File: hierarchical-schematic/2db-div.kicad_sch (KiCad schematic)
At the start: 28 parts, among them J1001 Conn_01x02, J1002 From R2, J1003 Conn_01x02, J1004 Out, SW1001 2dB, SW1002 Video, U1001 MC1458, U1002 MC1458

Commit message: hierarchical schematic updated to pass erc
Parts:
- removed U1001: MC1458, 2db-div:MC1458P, symbol Device:Opamp_Dual
- removed U1002: MC1458, 2db-div:MC1458P, symbol 2db-div:MC1458P
- added U1001: MC1458P, symbol spectrum analyzer:MC1458P
- D1001: symbol 2db-div:1N4152 -> Diode:1N4152
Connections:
- net GND: now also U1001.3 (+), U1001.5 (+)
- net at D1001.2 (A), R1003.1, R1007.2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: now also U1001.6 (-)
- net at D1001.1 (K), R1011.2, R1013.1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: now also U1001.7
- net at R1005.2, R1007.1, TP1001.1: now also U1001.1
- net at R1001.1, R1003.2: now also U1001.8 (V+)
- net at C1002.2, R1002.2: now also U1001.4 (V-)
- net at R1004.2, R1005.1: now also U1001.2 (-)

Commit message: v7 conversion
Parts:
- D1001: Spice_Lib_File 2db-div-spice\fairch.lib -> (none); Spice_Model 1N4152 -> (none); Spice_Netlist_Enabled Y -> (none); Spice_Node_Sequence 2 1 -> (none); Spice_Primitive D -> (none)
- J1001, J1003: Spice_Model Conn_01x02 -> (none); Spice_Netlist_Enabled N -> (none); Spice_Primitive J -> (none)
- J1004: Spice_Model Conn_Coaxial -> (none); Spice_Netlist_Enabled N -> (none); Spice_Primitive J -> (none)
- R1006: Spice_Lib_File 2db-div-spice\Pot.lib -> (none); Spice_Model pot_lin -> (none); Spice_Netlist_Enabled Y -> (none); Spice_Primitive X -> (none)
- R1012: Spice_Lib_File 2db-div-spice\Pot2.lib -> (none); Spice_Model pot_lin2 -> (none); Spice_Netlist_Enabled Y -> (none); Spice_Primitive X -> (none)
- SW1001: value 2dB -> ${SIM.PARAMS}; Spice_Netlist_Enabled N -> (none); Spice_Primitive R -> (none)
- TP1001: value 1458 Pin 1 -> ${SIM.PARAMS}; Spice_Netlist_Enabled N -> (none)
- TP1002: value 1458 Pin 7 -> ${SIM.PARAMS}; Spice_Netlist_Enabled N -> (none)

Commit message: Update to timebase and 2lo gerbers
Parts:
- J1002: symbol Connector:Conn_01x01_Female -> Connector:Conn_01x01_Socket
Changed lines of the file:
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@@
     )
   )
-  (symbol (lib_id "Connector:Conn_01x01_Female") (at 113.03 83.82 0) (mirror y) (unit 1)
+  (symbol (lib_id "Connector:Conn_01x01_Socket") (at 113.03 83.82 0) (mirror y) (unit 1)
     (in_bom yes) (on_board yes) (dnp no) (fields_autoplaced)
     (property "Reference" "J1002" (at 113.665 78.74 0)

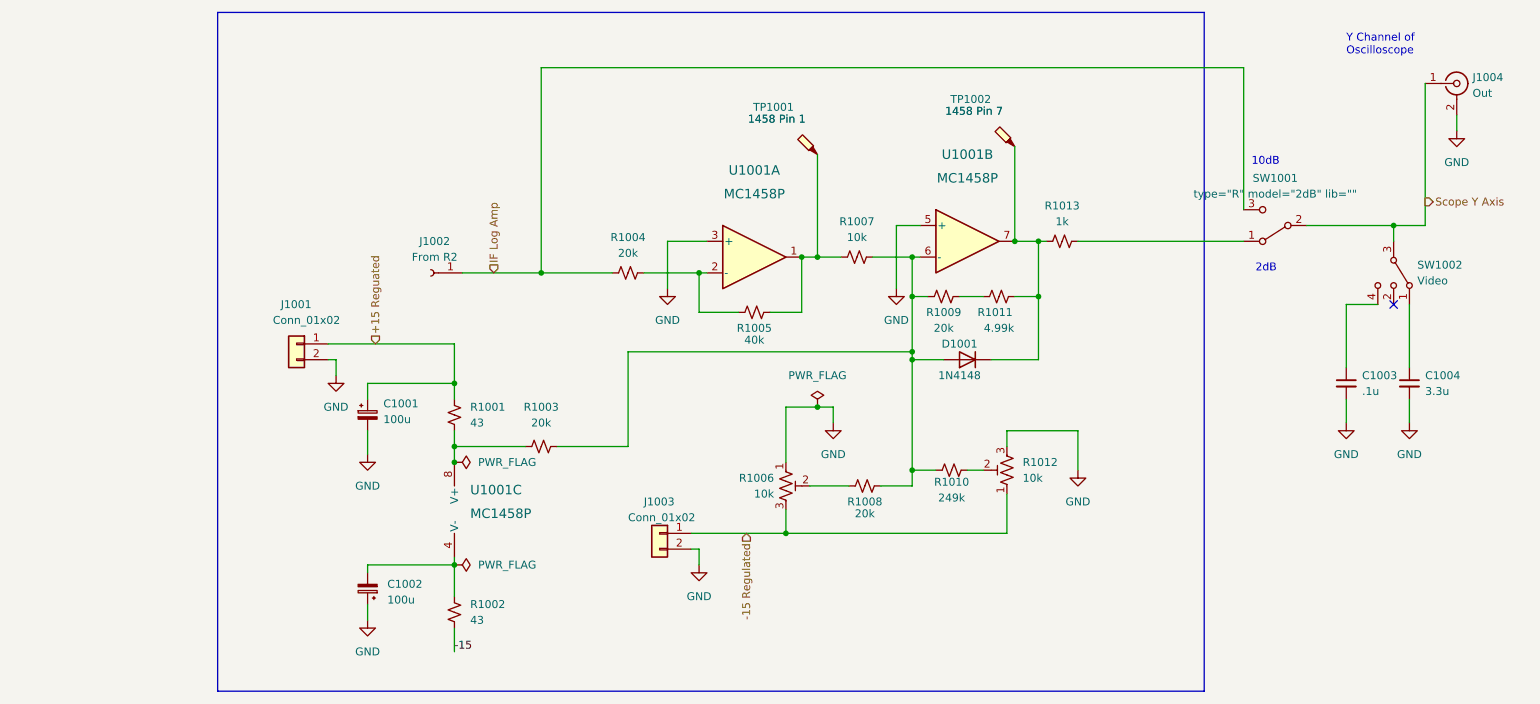
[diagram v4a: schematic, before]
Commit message: erc changes for hierarchical schematic
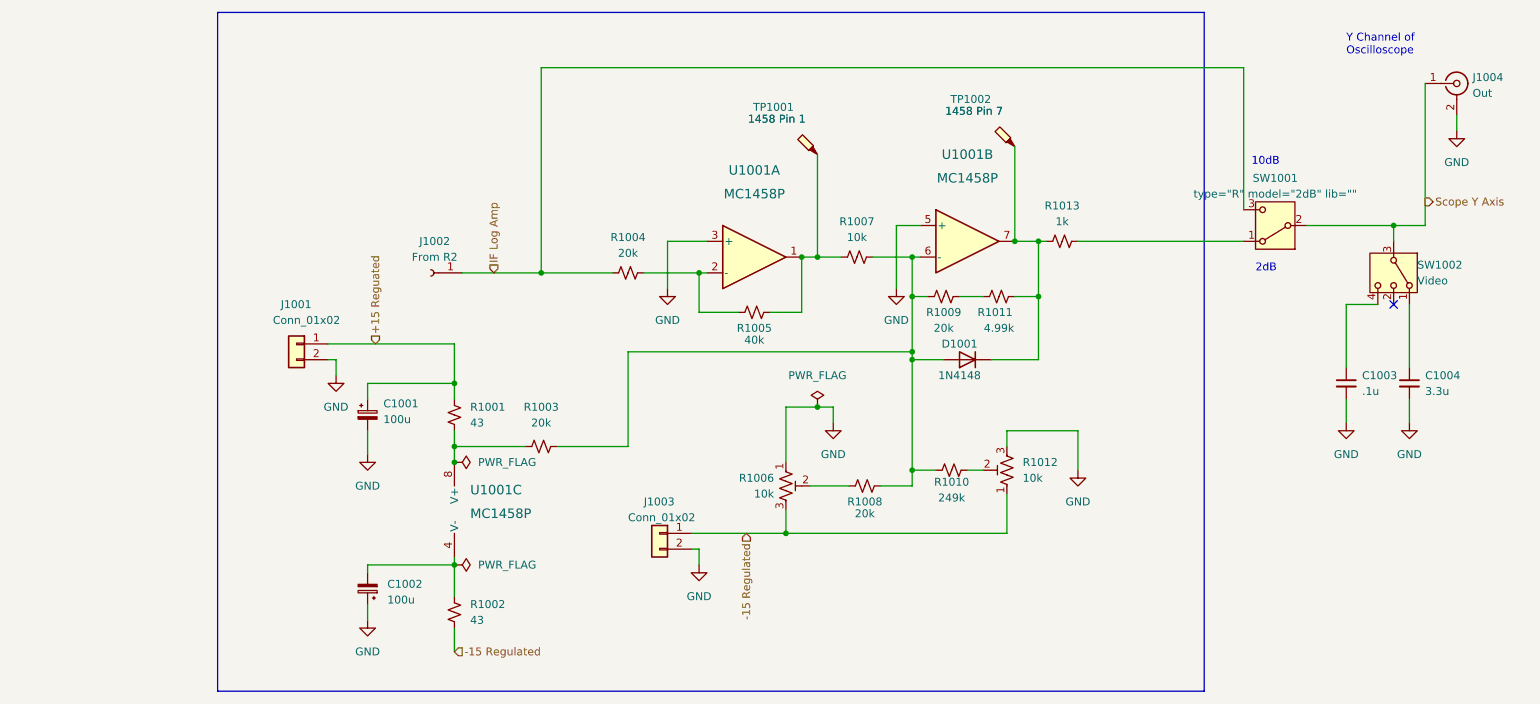
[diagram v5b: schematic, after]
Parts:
- D1001: symbol Diode:1N4152 -> Diode:1N4148
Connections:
- net -15 is gone; now on net -15 Regulated: R1002.1
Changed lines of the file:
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@@
-    (effects (font (size 1.27 1.27)) (justify left bottom))
-  )
-  (label "-15" (at 116.84 144.78 0) (fields_autoplaced)
     (effects (font (size 1.27 1.27)) (justify left bottom))
   )
@@
   )
   (hierarchical_label "IF Log Amp" (shape input) (at 123.19 83.82 90) (fields_autoplaced)
+    (effects (font (size 1.27 1.27)) (justify left))
+  )
+  (hierarchical_label "-15 Regulated" (shape input) (at 116.84 144.78 0) (fields_autoplaced)
     (effects (font (size 1.27 1.27)) (justify left))
   )
@@
     (property "Datasheet" " ~" (at 278.13 53.34 0)
       (effects (font (size 1.27 1.27)) hide)
-    )
-    (property "Sim.Enable" "0" (at 278.13 53.34 0)
-      (effects (font (size 1.27 1.27)) hide)
-    )
-    (property "Sim.Device" "SPICE" (at 278.13 53.34 0)
-      (effects (font (size 1.27 1.27)) hide)
-    )
-    (property "Sim.Params" "type=\"J\" model=\"Conn_Coaxial\" lib=\"\"" (at 0 0 0)
-      (effects (font (size 0 0)) hide)
-    )
-    (property "Sim.Pins" "1=1 2=2" (at 0 0 0)
-      (effects (font (size 0 0)) hide)
     )
     (pin "1")
@@
     )
   )
-  (symbol (lib_id "Diode:1N4152") (at 199.39 97.79 180) (unit 1)
+  (symbol (lib_id "Diode:1N4148") (at 199.39 97.79 180) (unit 1)
     (in_bom yes) (on_board yes) (dnp no)
     (property "Reference" "D1001" (at 198.12 95.25 0)
@@
       (effects (font (size 1.27 1.27)))
     )
-    (property "Footprint" "Diode_THT:D_DO-35_SOD27_P7.62mm_Horizontal" (at 199.39 93.345 0)
-      (effects (font (size 1.27 1.27)) hide)
-    )
-    (property "Datasheet" "" (at 199.39 97.79 0)
-      (effects (font (size 1.27 1.27)) hide)
-    )
-    (property "Sim.Device" "SPICE" (at 199.39 97.79 0)
+    (property "Footprint" "Diode_THT:D_DO-35_SOD27_P7.62mm_Horizontal" (at 199.39 97.79 0)
+      (effects (font (size 1.27 1.27)) hide)
+    )
+    (property "Datasheet" "https://assets.nexperia.com/documents/data-sheet/1N4148_1N4448.pdf" (at 199.39 97.79 0)
+      (effects (font (size 1.27 1.27)) hide)
+    )
+    (property "Sim.Device" "D" (at 199.39 97.79 0)
       (effects (font (size 1.27 1.27)) hide)
     )
@@
       (effects (font (size 0 0)) hide)
     )
-    (property "Sim.Pins" "2=1 1=2" (at 199.39 97.79 0)
-      (effects (font (size 1.27 1.27)) hide)
-    )
+    (property "Sim.Pins" "1=K 2=A" (at 199.39 97.79 0)
+      (effects (font (size 1.27 1.27)) hide)
+    )

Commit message: Added R2
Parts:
- added R2: R_Potentiometer_US, symbol Device:R_Potentiometer_US
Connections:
- net GND: now also R2.3
- net IF Log Amp: now also R2.1; no longer J1002.1 (Pin_1), R1004.1, SW1001.3 (C)
- new net: J1002.1 (Pin_1), R1004.1, R2.2, SW1001.3 (C)
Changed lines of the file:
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@@
   (junction (at 156.21 83.82) (diameter 0) (color 0 0 0 0)
+  )
+  (junction (at 118.11 83.82) (diameter 0) (color 0 0 0 0)
   )
   (no_connect (at 267.97 88.9))
@@
     (stroke (width 0) (type default))
   )
+  (wire (pts (xy 71.12 62.23) (xy 71.12 64.77))
+    (stroke (width 0) (type default))
+  )
   (wire (pts (xy 102.87 132.08) (xy 102.87 130.81))
     (stroke (width 0) (type default))
@@
     (stroke (width 0) (type default))
   )
+  (wire (pts (xy 118.11 68.58) (xy 74.93 68.58))
+    (stroke (width 0) (type default))
+  )
   (wire (pts (xy 154.94 125.73) (xy 170.18 125.73))
     (stroke (width 0) (type default))
@@
     (stroke (width 0) (type default))
   )
+  (wire (pts (xy 71.12 72.39) (xy 71.12 77.47))
+    (stroke (width 0) (type default))
+  )
   (wire (pts (xy 267.97 76.2) (xy 273.05 76.2))
     (stroke (width 0) (type default))
   )
   (wire (pts (xy 177.8 105.41) (xy 177.8 107.95))
+    (stroke (width 0) (type default))
+  )
+  (wire (pts (xy 118.11 83.82) (xy 118.11 68.58))
     (stroke (width 0) (type default))
   )
@@
     (effects (font (size 1.27 1.27)) (justify right))
   )
-  (hierarchical_label "IF Log Amp" (shape input) (at 123.19 83.82 90) (fields_autoplaced)
+  (hierarchical_label "IF Log Amp" (shape input) (at 71.12 62.23 90) (fields_autoplaced)
     (effects (font (size 1.27 1.27)) (justify left))
   )
@@
     )
   )
+  (symbol (lib_id "Device:R_Potentiometer_US") (at 71.12 68.58 0) (unit 1)
+    (in_bom yes) (on_board yes) (dnp no) (fields_autoplaced)
+    (property "Reference" "R2" (at 68.58 67.31 0)
+      (effects (font (size 1.27 1.27)) (justify right))
+    )
+    (property "Value" "R_Potentiometer_US" (at 68.58 69.85 0)
+      (effects (font (size 1.27 1.27)) (justify right))
+    )
+    (property "Footprint" "" (at 71.12 68.58 0)
+      (effects (font (size 1.27 1.27)) hide)
+    )
+    (property "Datasheet" "~" (at 71.12 68.58 0)
+      (effects (font (size 1.27 1.27)) hide)
+    )
+    (pin "3")
+    (pin "2")
+    (pin "1")
+    (instances
+      (project "W7ZOI Spectrum Analyzer"
+        (path "/d5173421-a214-4849-aa93-f108d8644c8a/6702cb80-1bae-4aa2-9f4a-d16d8c775e6d"
+          (reference "R2") (unit 1)
+        )
+      )
+    )
+  )
   (symbol (lib_id "power:GND") (at 260.35 107.95 0) (unit 1)
     (in_bom yes) (on_board yes) (dnp no) (fields_autoplaced)
@@
         )
       )
+    )
+  )
+  (symbol (lib_id "power:GND") (at 71.12 77.47 0) (unit 1)
+    (in_bom yes) (on_board yes) (dnp no) (fields_autoplaced)
+    (property "Reference" "#PWR0224" (at 71.12 83.82 0)
+      (effects (font (size 1.27 1.27)) hide)
+    )
+    (property "Value" "GND" (at 71.12 82.55 0)
+      (effects (font (size 1.27 1.27)))
+    )
+    (property "Footprint" "" (at 71.12 77.47 0)
+      (effects (font (size 1.27 1.27)) hide)
+    )
+    (property "Datasheet" "" (at 71.12 77.47 0)
+      (effects (font (size 1.27 1.27)) hide)
+    )
+    (pin "1")
+    (instances
+      (project "W7ZOI Spectrum Analyzer"
+        (path "/d5173421-a214-4849-aa93-f108d8644c8a/6702cb80-1bae-4aa2-9f4a-d16d8c775e6d"
+          (reference "#PWR0224") (unit 1)
+        )
+      )

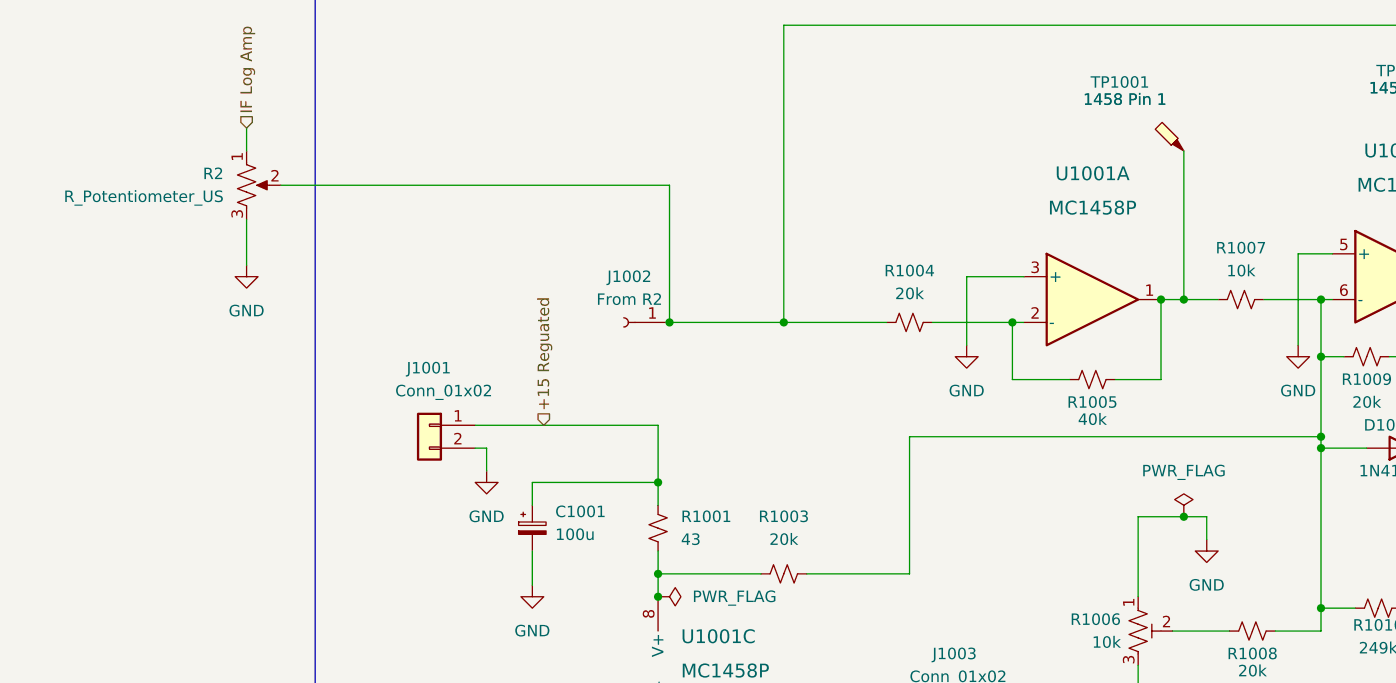
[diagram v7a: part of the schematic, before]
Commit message: updatess to kicad v8
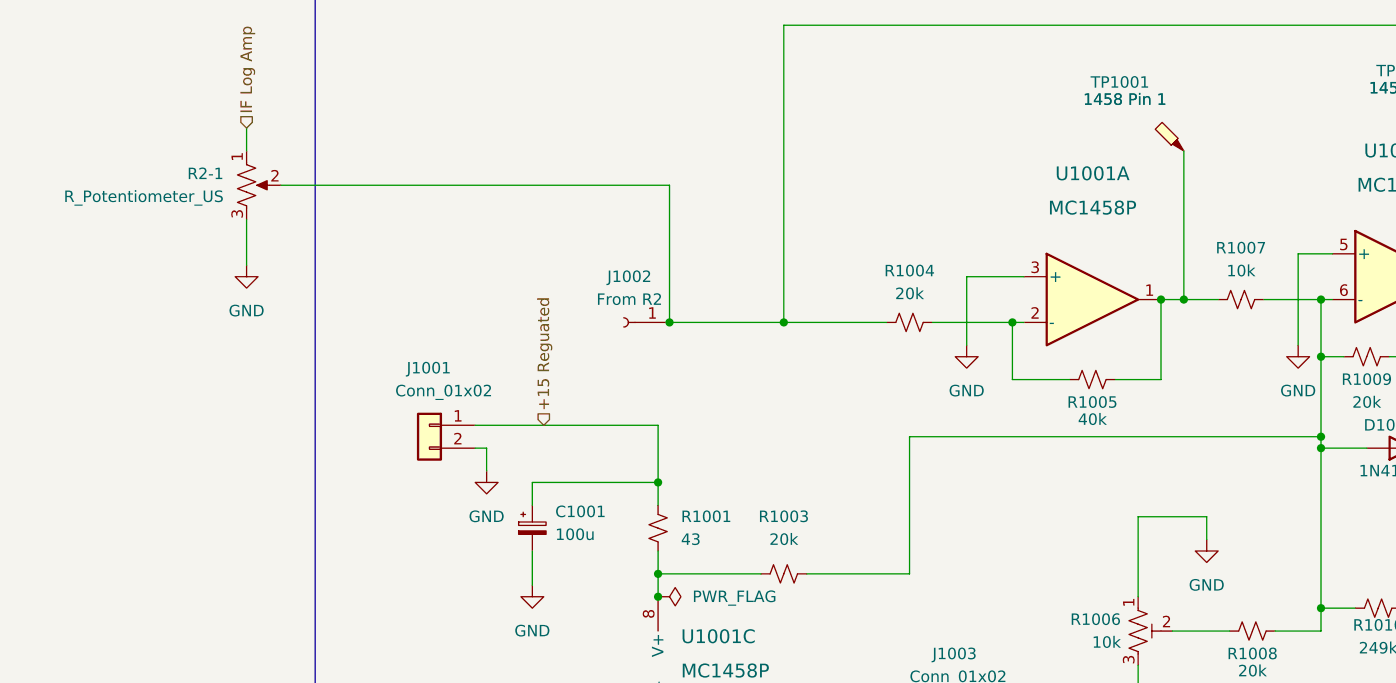
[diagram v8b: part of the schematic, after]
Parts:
- renumbered R2 to R2-1
